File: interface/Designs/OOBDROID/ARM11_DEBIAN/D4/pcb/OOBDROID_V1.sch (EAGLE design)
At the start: 37 parts, among them T1 BC847, T2 BC817, U1 MCP2551, U2 MCP2551, X1 16MHz, X2 ODROID P1, X3 16MHz, X4 ODROID-P5

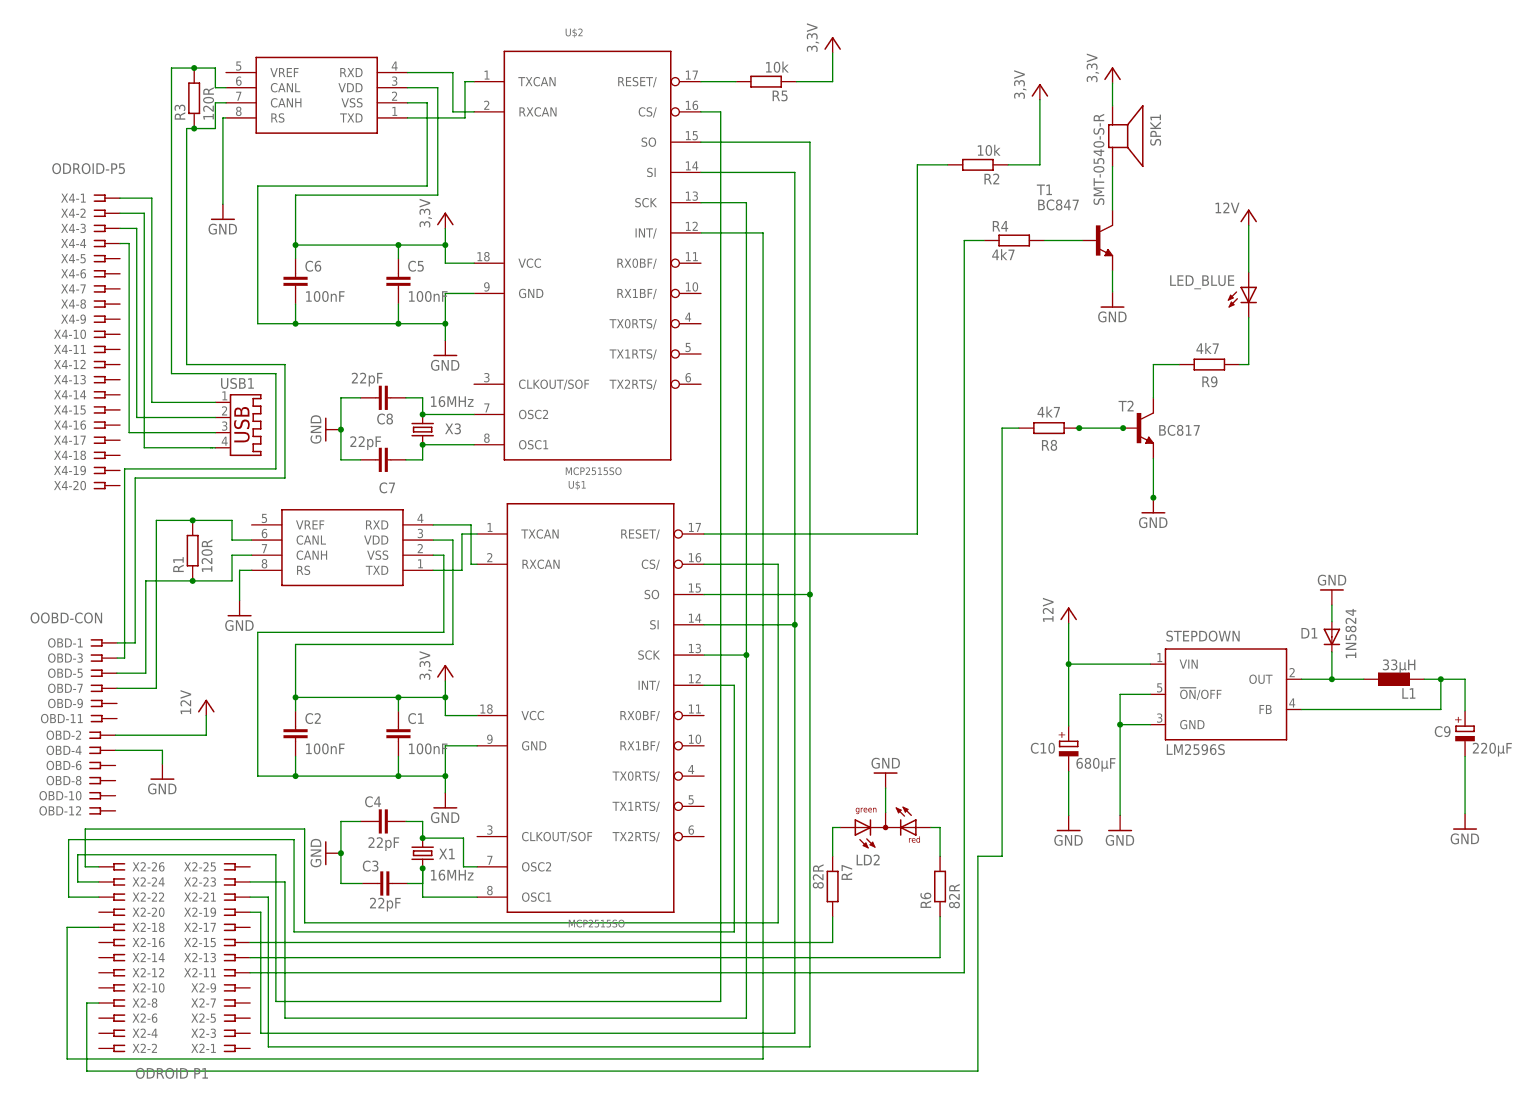
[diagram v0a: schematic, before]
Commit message: add latest PCB/schematics modification for OOBDROID extension
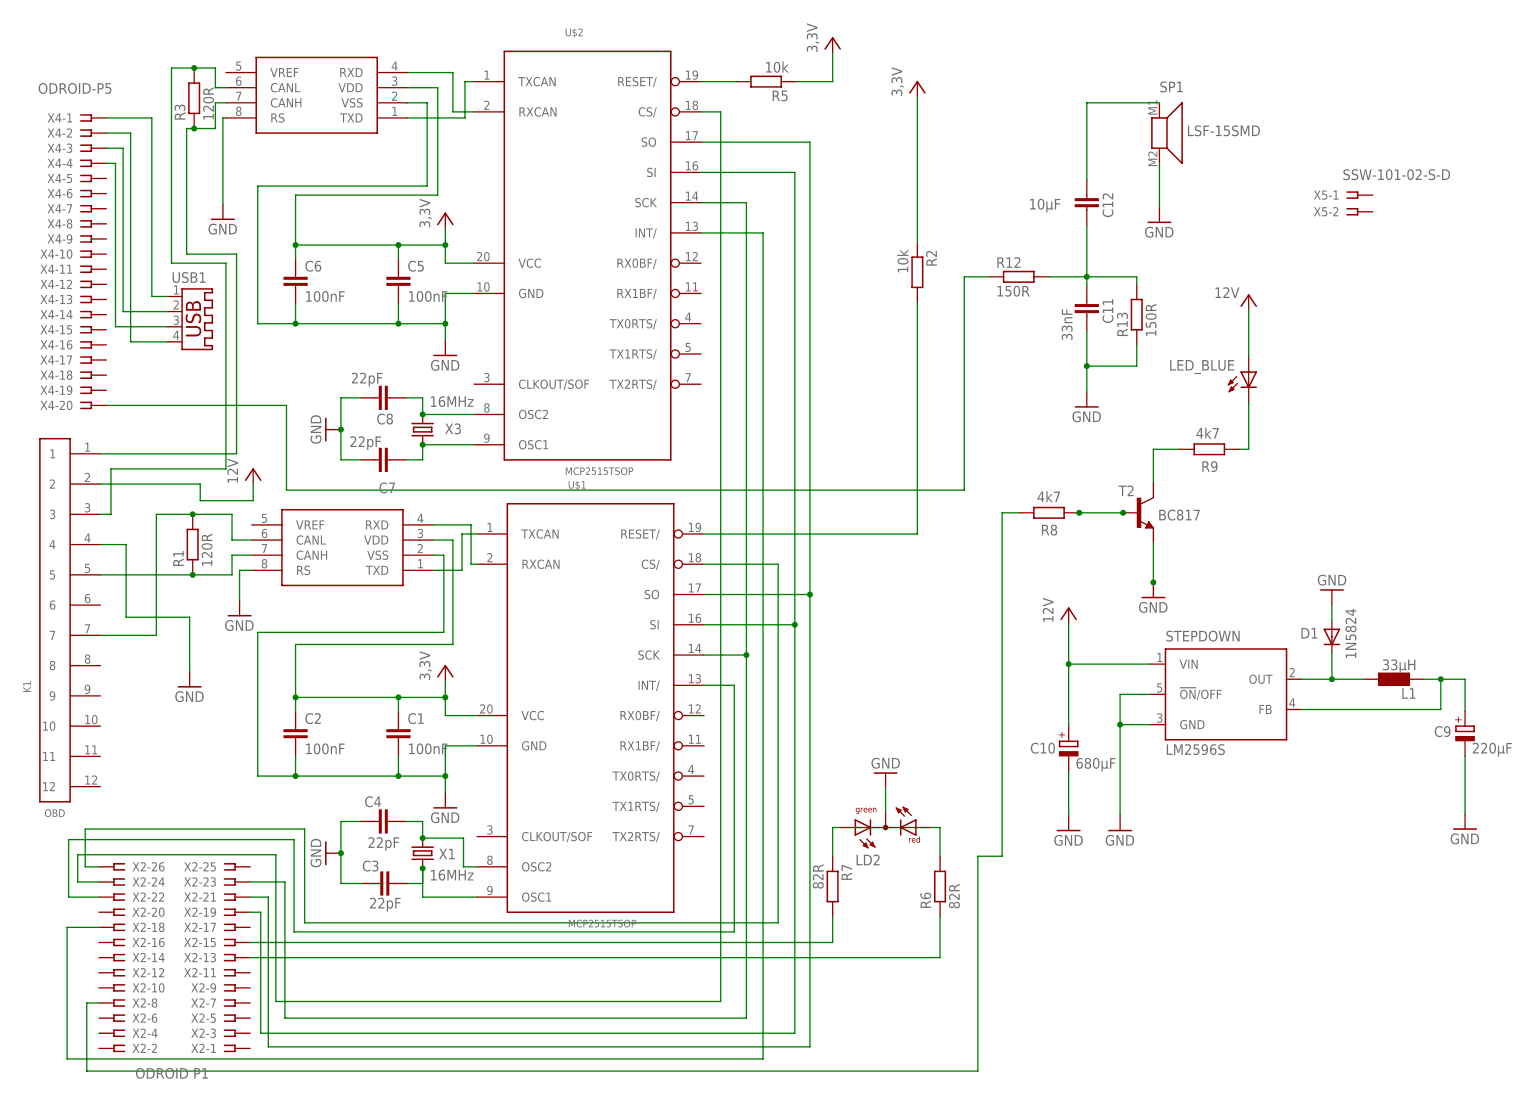
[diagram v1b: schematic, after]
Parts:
- removed OBD: OOBD-CON, con-samtec:SSW-106-02-S-D
- removed R4: 4k7, eagle-ltspice:RR0603
- removed SPK1: SMT-0540-S-R, adafruit:SMT-0540-S-R
- removed T1: BC847, transistor:BC847
- added C11: 33nF, eagle-ltspice:C
- added C12: 10µF, eagle-ltspice:C
- added K1: OBD, EagleLibrary_Wuerth_Elektronik _eiCan_Wire_to_Board_Connectors_v6_20150113:653112124022
- added R12, R13: 150R, eagle-ltspice:RR0603
- added SP1: LSF-15SMD, speaker:SMS-1308MS-2-RLSF-15SMD
- added X5: SSW-101-02-S-D, con-samtec:SSW-101-02-S-D
- U$1, U$2: value MCP2515SO -> MCP2515TSOP; device MCP2515_MT:MCP2515SO -> MCP2515_MT:MCP2515TSOP
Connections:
- removed net N$20: SPK1.-, T1.C
- removed net N$21: R4.2, T1.B
- new net N$17: C12.2, SP1.1
- new net N$37: C11.2, C12.1, R12.2, R13.2
- net GND: now also C11.1, K1.4, R13.1, SP1.2; no longer OBD-4.1, T1.E
- net N$1: now also K1.5; no longer OBD-5.1
- net N$10: now also K1.1; no longer OBD-1.1
- net N$16: now also K1.7; no longer OBD-7.1
- net N$30: now also R12.1, X4-20.1; no longer R4.1, X2-11.1
- net N$9: now also K1.3; no longer OBD-3.1
- net VCC: now also K1.2; no longer OBD-2.1, SPK1.+
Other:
- moved on the sheet: LED_BLUE, R1, R2, R8, R9, T2, USB1, X4-1, X4-10, X4-11, X4-12, X4-13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

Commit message: add latest modifcation of OOBDROID to new feature branch
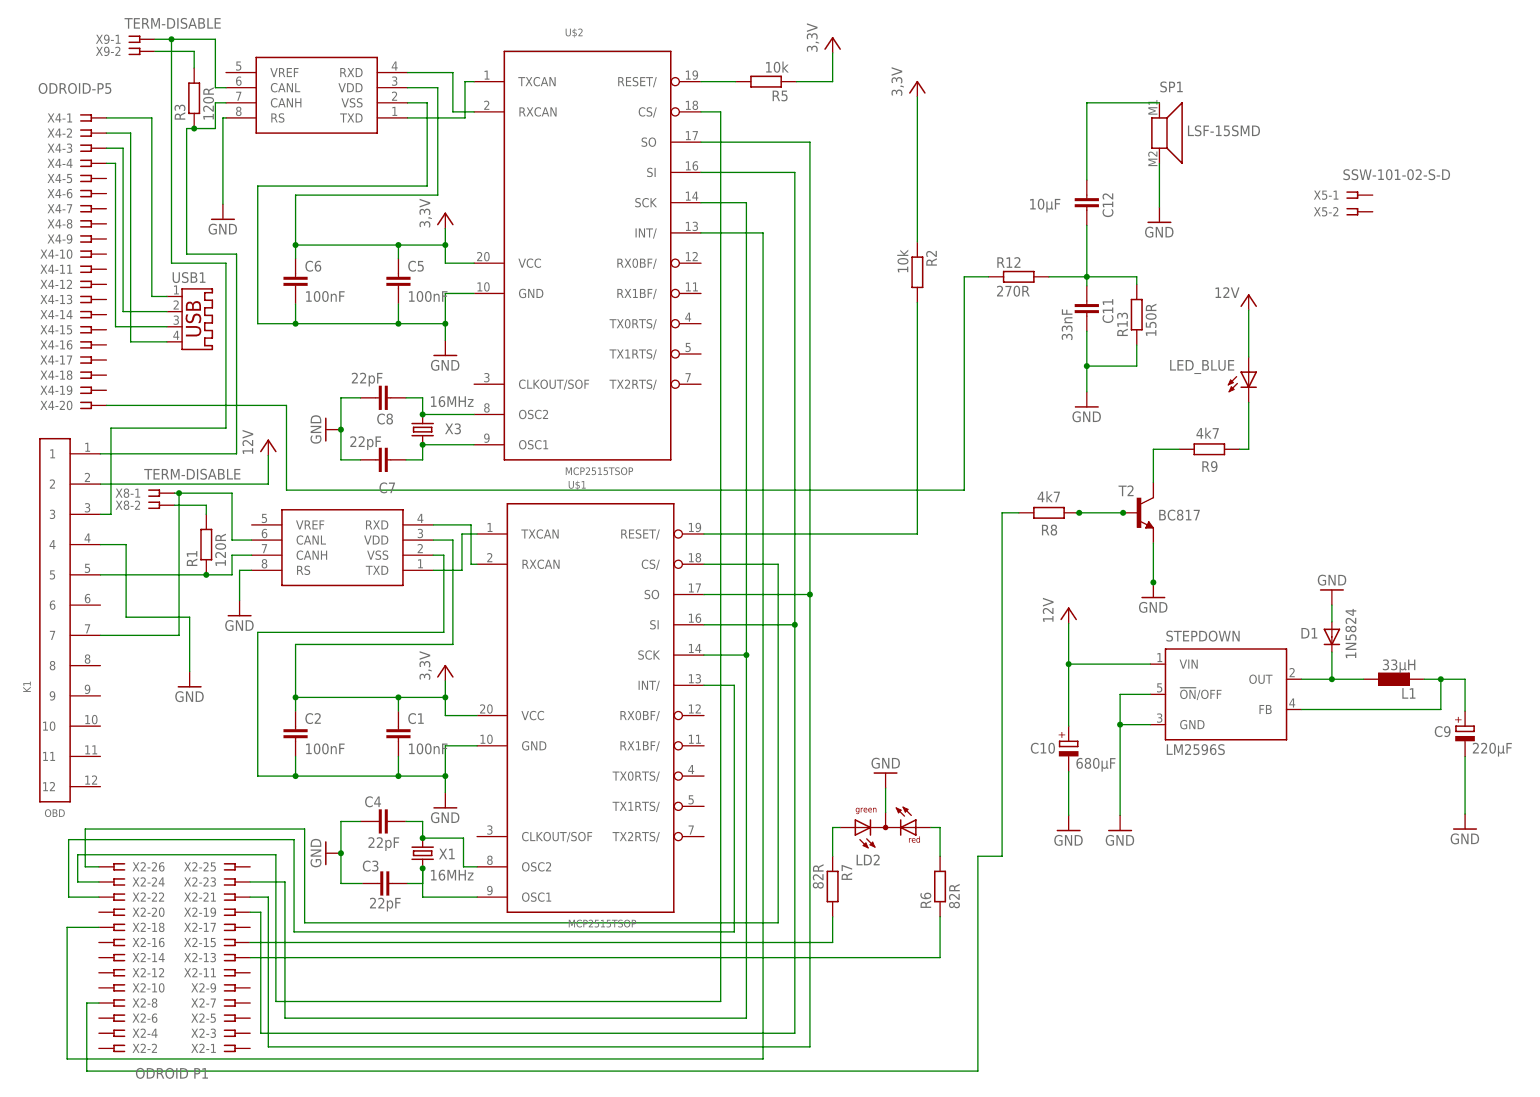
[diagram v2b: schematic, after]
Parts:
- added X8, X9: TERM-DISABLE, con-samtec:SSW-101-02-S-D
- R12: value 150R -> 270R
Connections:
- new net N$21: R3.2, X9-2.1
- new net N$39: R1.2, X8-2.1
- net N$16: now also X8-1.1; no longer R1.2
- net N$9: now also X9-1.1; no longer R3.2
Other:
- moved on the sheet: R1
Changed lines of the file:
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@@
 <setting verticaltext="up"/>
 </settings>
-<grid distance="10" unitdist="mil" unit="mil" style="lines" multiple="1" display="no" altdistance="1" altunitdist="mil" altunit="mil"/>
+<grid distance="0.1" unitdist="inch" unit="inch" style="lines" multiple="1" display="no" altdistance="0.01" altunitdist="inch" altunit="inch"/>
 <layers>
 <layer number="1" name="Top" color="4" fill="1" visible="no" active="no"/>
@@
 <part name="K1" library="EagleLibrary_Wuerth_Elektronik _eiCan_Wire_to_Board_Connectors_v6_20150113" deviceset="653112124022" device="" value="OBD"/>
 <part name="C12" library="eagle-ltspice" deviceset="C" device="" value="10µF"/>
-<part name="R12" library="eagle-ltspice" deviceset="R" device="R0603" value="150R"/>
+<part name="R12" library="eagle-ltspice" deviceset="R" device="R0603" value="270R"/>
 <part name="R13" library="eagle-ltspice" deviceset="R" device="R0603" value="150R"/>
 <part name="C11" library="eagle-ltspice" deviceset="C" device="" value="33nF"/>
@@
 <part name="GND15" library="supply1" deviceset="GND" device=""/>
 <part name="X5" library="con-samtec" deviceset="SSW-101-02-S-D" device=""/>
+<part name="X8" library="con-samtec" deviceset="SSW-101-02-S-D" device="" value="TERM-DISABLE">
+<attribute name="MPN" value="CAN-DISABLE"/>
+</part>
+<part name="X9" library="con-samtec" deviceset="SSW-101-02-S-D" device="" value="TERM-DISABLE"/>
 </parts>
 <sheets>
@@
 <instance part="U$1" gate="G$1" x="-11.43" y="6.604"/>
 <instance part="C1" gate="G$1" x="-42.418" y="2.286"/>
-<instance part="R1" gate="G$1" x="-76.962" y="32.766" rot="R90"/>
+<instance part="R1" gate="G$1" x="-74.676" y="32.766" rot="R90"/>
 <instance part="C2" gate="G$1" x="-59.69" y="2.286"/>
 <instance part="C3" gate="G$1" x="-45.974" y="-24.13" smashed="yes" rot="R90">
@@
 <instance part="GND12" gate="1" x="39.37" y="-5.588" rot="R180"/>
 <instance part="GND13" gate="1" x="-77.47" y="8.89"/>
-<instance part="P+7" gate="VCC" x="-66.802" y="45.466"/>
+<instance part="P+7" gate="VCC" x="-64.262" y="50.292"/>
 <instance part="X2" gate="-1" x="-69.85" y="-51.816" smashed="yes" rot="MR180">
 <attribute name="VALUE" x="-86.614" y="-55.118" size="1.778" layer="96" rot="MR180"/>
@@
 <instance part="X5" gate="-1" x="118.618" y="91.44"/>
 <instance part="X5" gate="-2" x="118.618" y="88.646"/>
+<instance part="X8" gate="-1" x="-82.55" y="41.402" smashed="yes">
+<attribute name="VALUE" x="-85.09" y="43.688" size="1.778" layer="96"/>
+<attribute name="NAME" x="-85.598" y="42.164" size="1.524" layer="95" rot="R180"/>
+</instance>
+<instance part="X8" gate="-2" x="-82.55" y="39.37"/>
+<instance part="X9" gate="-1" x="-85.852" y="117.602" smashed="yes">
+<attribute name="VALUE" x="-88.392" y="119.38" size="1.778" layer="96"/>
+<attribute name="NAME" x="-88.9" y="118.364" size="1.524" layer="95" rot="R180"/>
+</instance>
+<instance part="X9" gate="-2" x="-85.852" y="115.57"/>
 </instances>
 <busses>
@@
 <pinref part="P+7" gate="VCC" pin="VCC"/>
 <pinref part="K1" gate="G$1" pin="2"/>
-<wire x1="-66.802" y1="42.926" x2="-66.802" y2="40.132" width="0.1524" layer="91"/>
-<wire x1="-66.802" y1="40.132" x2="-75.692" y2="40.132" width="0.1524" layer="91"/>
-<wire x1="-75.692" y1="40.132" x2="-75.692" y2="42.926" width="0.1524" layer="91"/>
-<wire x1="-75.692" y1="42.926" x2="-92.456" y2="42.926" width="0.1524" layer="91"/>
+<wire x1="-64.262" y1="47.752" x2="-64.262" y2="42.926" width="0.1524" layer="91"/>
+<wire x1="-64.262" y1="42.926" x2="-92.456" y2="42.926" width="0.1524" layer="91"/>
 </segment>
 <segment>
@@
 <net name="N$9" class="0">
 <segment>
+<wire x1="-80.518" y1="117.602" x2="-80.518" y2="80.01" width="0.1524" layer="91"/>
+<wire x1="-80.518" y1="80.01" x2="-71.374" y2="80.01" width="0.1524" layer="91"/>
+<wire x1="-71.374" y1="80.01" x2="-71.374" y2="52.324" width="0.1524" layer="91"/>
+<wire x1="-71.374" y1="52.324" x2="-90.678" y2="52.324" width="0.1524" layer="91"/>
+<wire x1="-90.678" y1="52.324" x2="-90.678" y2="37.846" width="0.1524" layer="91"/>
+<wire x1="-92.456" y1="37.846" x2="-90.678" y2="37.846" width="0.1524" layer="91"/>
+<pinref part="K1" gate="G$1" pin="3"/>
 <pinref part="U2" gate="G$1" pin="CANL"/>
 <wire x1="-71.374" y1="109.474" x2="-73.152" y2="109.474" width="0.1524" layer="91"/>
-<wire x1="-73.152" y1="109.474" x2="-73.152" y2="112.776" width="0.1524" layer="91"/>
-<wire x1="-73.152" y1="112.776" x2="-76.708" y2="112.776" width="0.1524" layer="91"/>
-<pinref part="R3" gate="G$1" pin="2"/>
-<junction x="-76.708" y="112.776"/>
-<wire x1="-76.708" y1="112.776" x2="-80.518" y2="112.776" width="0.1524" layer="91"/>
-<wire x1="-80.518" y1="112.776" x2="-80.518" y2="80.01" width="0.1524" layer="91"/>
-<wire x1="-80.518" y1="80.01" x2="-71.374" y2="80.01" width="0.1524" layer="91"/>
-<wire x1="-71.374" y1="80.01" x2="-71.374" y2="45.466" width="0.1524" layer="91"/>
-<wire x1="-71.374" y1="45.466" x2="-90.678" y2="45.466" width="0.1524" layer="91"/>
-<wire x1="-90.678" y1="45.466" x2="-90.678" y2="37.846" width="0.1524" layer="91"/>
-<wire x1="-92.456" y1="37.846" x2="-90.678" y2="37.846" width="0.1524" layer="91"/>
-<pinref part="K1" gate="G$1" pin="3"/>
+<pinref part="X9" gate="-1" pin="1"/>
+<wire x1="-73.152" y1="109.474" x2="-73.152" y2="117.602" width="0.1524" layer="91"/>
+<wire x1="-73.152" y1="117.602" x2="-80.518" y2="117.602" width="0.1524" layer="91"/>
+<wire x1="-80.518" y1="117.602" x2="-83.312" y2="117.602" width="0.1524" layer="91"/>
+<junction x="-80.518" y="117.602"/>
 </segment>
 </net>
@@
 <net name="N$16" class="0">
 <segment>
+<wire x1="-79.248" y1="41.402" x2="-79.248" y2="17.526" width="0.1524" layer="91"/>
+<wire x1="-79.248" y1="17.526" x2="-92.456" y2="17.526" width="0.1524" layer="91"/>
+<pinref part="K1" gate="G$1" pin="7"/>
 <pinref part="U1" gate="G$1" pin="CANL"/>
 <wire x1="-67.056" y1="33.528" x2="-70.358" y2="33.528" width="0.1524" layer="91"/>
-<wire x1="-70.358" y1="33.528" x2="-70.358" y2="37.846" width="0.1524" layer="91"/>
-<wire x1="-70.358" y1="37.846" x2="-76.962" y2="37.846" width="0.1524" layer="91"/>
-<pinref part="R1" gate="G$1" pin="2"/>
-<junction x="-76.962" y="37.846"/>
-<wire x1="-76.962" y1="37.846" x2="-83.058" y2="37.846" width="0.1524" layer="91"/>
-<wire x1="-83.058" y1="37.846" x2="-83.058" y2="17.526" width="0.1524" layer="91"/>
-<wire x1="-83.058" y1="17.526" x2="-92.456" y2="17.526" width="0.1524" layer="91"/>
-<pinref part="K1" gate="G$1" pin="7"/>
+<wire x1="-70.358" y1="33.528" x2="-70.358" y2="41.402" width="0.1524" layer="91"/>
+<pinref part="X8" gate="-1" pin="1"/>
+<wire x1="-80.01" y1="41.402" x2="-79.248" y2="41.402" width="0.1524" layer="91"/>
+<wire x1="-79.248" y1="41.402" x2="-70.358" y2="41.402" width="0.1524" layer="91"/>
+<junction x="-79.248" y="41.402"/>
 </segment>
 </net>
@@
 <wire x1="-67.056" y1="30.988" x2="-70.358" y2="30.988" width="0.1524" layer="91"/>
 <wire x1="-70.358" y1="30.988" x2="-70.358" y2="27.686" width="0.1524" layer="91"/>
-<wire x1="-70.358" y1="27.686" x2="-76.962" y2="27.686" width="0.1524" layer="91"/>
+<wire x1="-70.358" y1="27.686" x2="-74.676" y2="27.686" width="0.1524" layer="91"/>
 <pinref part="R1" gate="G$1" pin="1"/>
-<junction x="-76.962" y="27.686"/>
+<junction x="-74.676" y="27.686"/>
 <pinref part="U1" gate="G$1" pin="CANH"/>
 <pinref part="K1" gate="G$1" pin="5"/>
-<wire x1="-92.456" y1="27.686" x2="-76.962" y2="27.686" width="0.1524" layer="91"/>
+<wire x1="-92.456" y1="27.686" x2="-74.676" y2="27.686" width="0.1524" layer="91"/>
 </segment>
 </net>
@@
 </segment>
 </net>
+<net name="N$39" class="0">
+<segment>
+<pinref part="R1" gate="G$1" pin="2"/>
+<pinref part="X8" gate="-2" pin="1"/>
+<wire x1="-80.01" y1="39.37" x2="-74.676" y2="39.37" width="0.1524" layer="91"/>
+<wire x1="-74.676" y1="39.37" x2="-74.676" y2="37.846" width="0.1524" layer="91"/>
+</segment>
+</net>
+<net name="N$21" class="0">
+<segment>
+<pinref part="R3" gate="G$1" pin="2"/>
+<wire x1="-76.708" y1="115.57" x2="-76.708" y2="112.776" width="0.1524" layer="91"/>
+<pinref part="X9" gate="-2" pin="1"/>
+<wire x1="-83.312" y1="115.57" x2="-76.708" y2="115.57" width="0.1524" layer="91"/>
+</segment>
+</net>
